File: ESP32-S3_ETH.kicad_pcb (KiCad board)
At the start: 2 copper layers, 147.4 x 97.9 mm, 20 parts, among them J1 Screw_Terminal_01x02, J2 Screw_Terminal_01x04, J3 SSW-104-01-F-S, J4 SSW-108-02-G-D, J5 Screw_Terminal_01x03, J6 Screw_Terminal_01x03, J7 SSW-120-01-X-S, J8 SSW-120-01-X-S, U1 ESP32-S3-ETH

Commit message: v1 ok
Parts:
- moved H4 27.0 mm to (106.9, 136.9)
- moved H1 26.9 mm to (106.8, 52.1)
- moved J6 4.26 mm to (158.8, 127.0)
- moved J1 2.30 mm to (141.4, 127.0)
- moved J2 1.10 mm to (180.8, 127.0)
- moved J5 0.35 mm to (119.0, 127.1)
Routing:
- net GND: track 0.00 -> 202.8 mm, vias 0 -> 27
- net +3V3: track 0.00 -> 192.8 mm, vias 0 -> 1
- net Net-(J5-Pin_2): track 0.00 -> 102.6 mm, vias 0 -> 1
- net +5V: track 0.00 -> 97.9 mm, vias 0 -> 1
- net Net-(U1-GPIO34): track 0.00 -> 92.7 mm, vias 0 -> 1
- net Net-(U1-GPIO33): track 0.00 -> 85.3 mm, vias 0 -> 1
- net Net-(U1-GPIO37): track 0.00 -> 80.5 mm, vias 0 -> 1
- net Net-(U1-GPIO42): track 0.00 -> 77.9 mm
- net Net-(U1-GPIO35): track 0.00 -> 77.5 mm, vias 0 -> 1
- net Net-(U1-GPIO36): track 0.00 -> 74.7 mm, vias 0 -> 1
- net Net-(U1-GPIO41): track 0.00 -> 73.1 mm
- net Net-(U1-GPIO40): track 0.00 -> 72.9 mm, vias 0 -> 1
- net Net-(U1-GPIO38): track 0.00 -> 63.6 mm, vias 0 -> 2
- net Net-(U1-GPIO17): track 0.00 -> 51.4 mm, vias 0 -> 1
- net Net-(U1-GPIO47/CSI_SIOC): track 0.00 -> 51.3 mm, vias 0 -> 2
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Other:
- board size 147.4 x 97.9 mm -> 122.1 x 97.9 mm

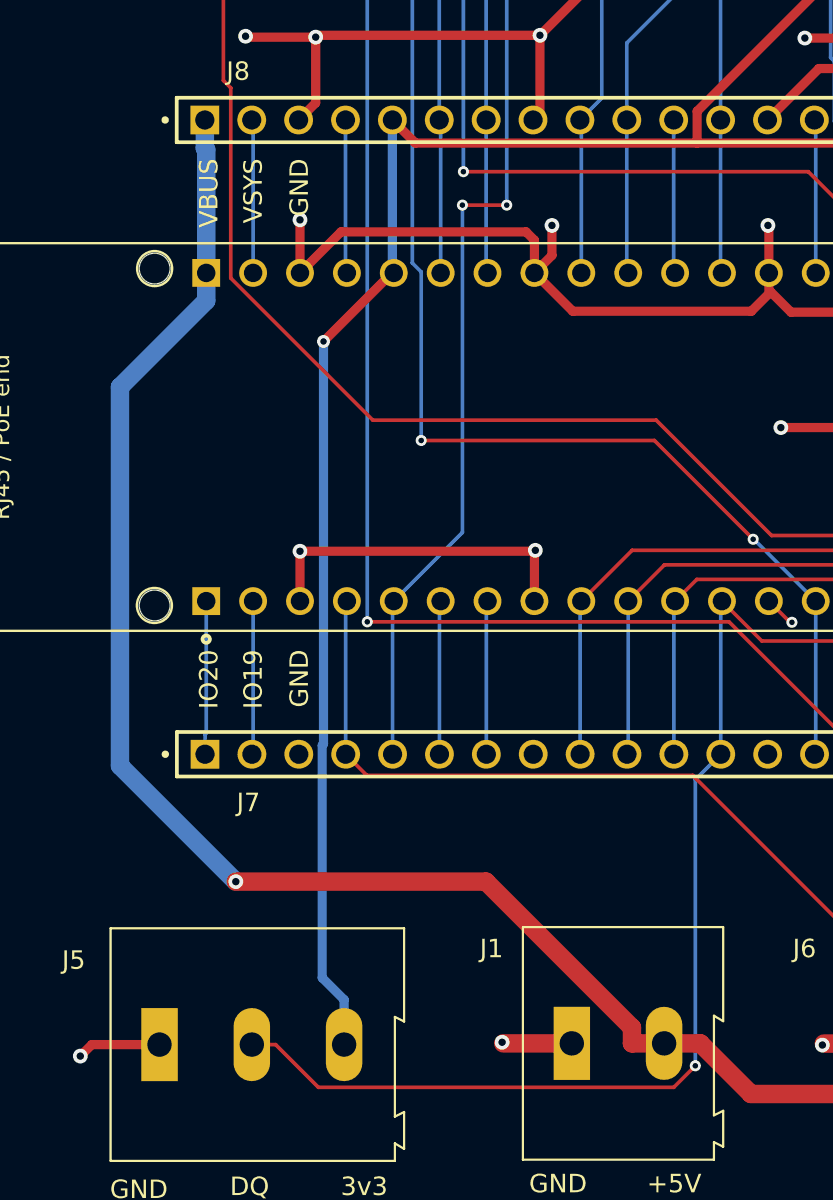
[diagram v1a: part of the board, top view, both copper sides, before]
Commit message: Cleanup track and vias
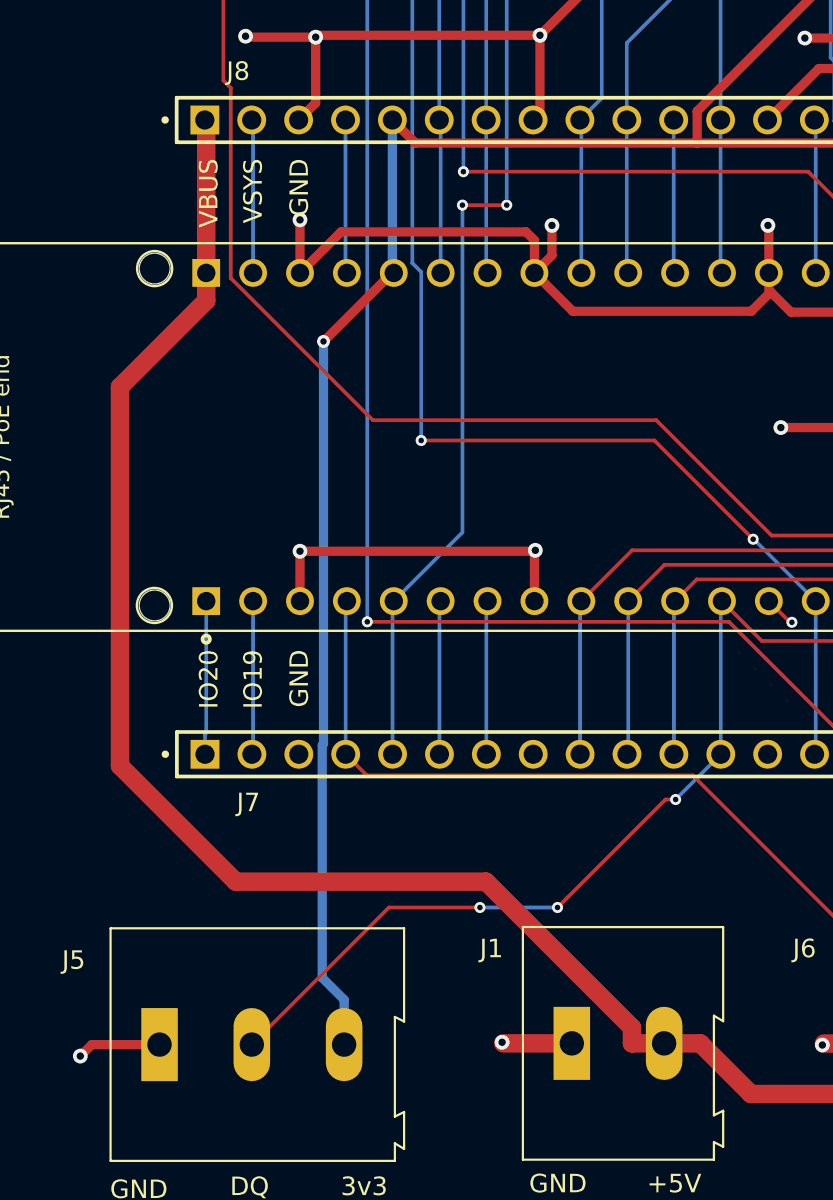
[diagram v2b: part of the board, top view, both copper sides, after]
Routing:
- net Net-(J5-Pin_2): track 102.6 -> 91.6 mm, vias 1 -> 3
- net +5V: track 97.9 -> 97.8 mm, vias 1 -> 0
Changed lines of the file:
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@@
+	)
+	(segment
+		(start 121.57 77.0625)
+		(end 121.57 85.2725)
+		(width 1)
+		(layer "F.Cu")
+		(net "+5V")
+	)
+	(segment
+		(start 116.8983 111.9741)
+		(end 123.1734 118.2492)
+		(width 1)
+		(layer "F.Cu")
+		(net "+5V")
 	)
 	(segment
@@
 	)
 	(segment
+		(start 121.57 86.7782)
+		(end 116.8983 91.4499)
+		(width 1)
+		(layer "F.Cu")
+		(net "+5V")
+	)
+	(segment
+		(start 121.57 85.2725)
+		(end 121.57 86.7782)
+		(width 1)
+		(layer "F.Cu")
+		(net "+5V")
+	)
+	(segment
 		(start 146.375 127.01)
 		(end 148.3387 127.01)
@@
 	)
 	(segment
+		(start 116.8983 91.4499)
+		(end 116.8983 111.9741)
+		(width 1)
+		(layer "F.Cu")
+		(net "+5V")
+	)
+	(segment
 		(start 123.1734 118.2492)
 		(end 136.7283 118.2492)
@@
 		(net "+5V")
 	)
-	(via
-		(at 123.1734 118.2492)
-		(size 0.8)
-		(drill 0.4)
-		(layers "F.Cu" "B.Cu")
-		(net "+5V")
-	)
-	(segment
-		(start 121.495 78.5192)
-		(end 121.57 78.5942)
-		(width 1)
-		(layer "B.Cu")
-		(net "+5V")
-	)
-	(segment
-		(start 121.495 76.9875)
-		(end 121.495 78.5192)
-		(width 1)
-		(layer "B.Cu")
-		(net "+5V")
-	)
-	(segment
-		(start 116.8983 111.9741)
-		(end 123.1734 118.2492)
-		(width 1)
-		(layer "B.Cu")
-		(net "+5V")
-	)
-	(segment
-		(start 121.57 86.7782)
-		(end 116.8983 91.4499)
-		(width 1)
-		(layer "B.Cu")
-		(net "+5V")
-	)
-	(segment
-		(start 121.57 85.2725)
-		(end 121.57 86.7782)
-		(width 1)
-		(layer "B.Cu")
-		(net "+5V")
-	)
-	(segment
-		(start 116.8983 91.4499)
-		(end 116.8983 111.9741)
-		(width 1)
-		(layer "B.Cu")
-		(net "+5V")
-	)
-	(segment
-		(start 121.57 78.5942)
-		(end 121.57 85.2725)
-		(width 1)
-		(layer "B.Cu")
-		(net "+5V")
-	)
 	(segment
 		(start 124.11 77.0625)
@@
 	)
 	(segment
-		(start 146.8989 129.3924)
-		(end 148.0663 128.225)
+		(start 146.45 113.8)
+		(end 147 113.8)
 		(width 0.2)
 		(layer "F.Cu")
@@
 	)
 	(segment
-		(start 125.3317 127.0766)
-		(end 127.6475 129.3924)
+		(start 131.4666 119.65)
+		(end 136.4 119.65)
 		(width 0.2)
 		(layer "F.Cu")
@@
 	)
 	(segment
-		(start 127.6475 129.3924)
-		(end 146.8989 129.3924)
-		(width 0.2)
-		(layer "F.Cu")
-		(net "Net-(J5-Pin_2)")
-	)
-	(segment
-		(start 124.04 127.0766)
-		(end 125.3317 127.0766)
+		(start 140.6 119.65)
+		(end 146.45 113.8)
 		(width 0.2)
 		(layer "F.Cu")
@@
 		(net "Net-(J5-Pin_2)")
 	)
-	(via
-		(at 148.0663 128.225)
-		(size 0.6)
-		(drill 0.3)
-		(layers "F.Cu" "B.Cu")
+	(segment
+		(start 124.04 127.0766)
+		(end 131.4666 119.65)
+		(width 0.2)
+		(layer "F.Cu")
+		(net "Net-(J5-Pin_2)")
+	)
+	(via
+		(at 147 113.8)
+		(size 0.6)
+		(drill 0.3)
+		(layers "F.Cu" "B.Cu")
+		(net "Net-(J5-Pin_2)")
+	)
+	(via
+		(at 140.6 119.65)
+		(size 0.6)
+		(drill 0.3)
+		(layers "F.Cu" "B.Cu")
+		(net "Net-(J5-Pin_2)")
+	)
+	(via
+		(at 136.4 119.65)
+		(size 0.6)
+		(drill 0.3)
+		(layers "F.Cu" "B.Cu")
+		(net "Net-(J5-Pin_2)")
+	)
+	(segment
+		(start 136.4 119.65)
+		(end 140.6 119.65)
+		(width 0.2)
+		(layer "B.Cu")
 		(net "Net-(J5-Pin_2)")
 	)
@@
 	)
 	(segment
-		(start 148.0663 112.7262)
+		(start 147 113.7925)
 		(end 149.445 111.3475)
 		(width 0.2)
@@
 	)
 	(segment
-		(start 148.0663 128.225)
-		(end 148.0663 112.7262)
-		(width 0.2)
-		(layer "B.Cu")
+		(start 147 113.8)
+		(end 147 113.7925)
+		(width 0.2)
+		(layer "B.Cu")
